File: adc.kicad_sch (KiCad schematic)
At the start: 87 parts, among them U35 MCP6004, U36 MCP6004, U46 MCP6004, U8 MCP6004

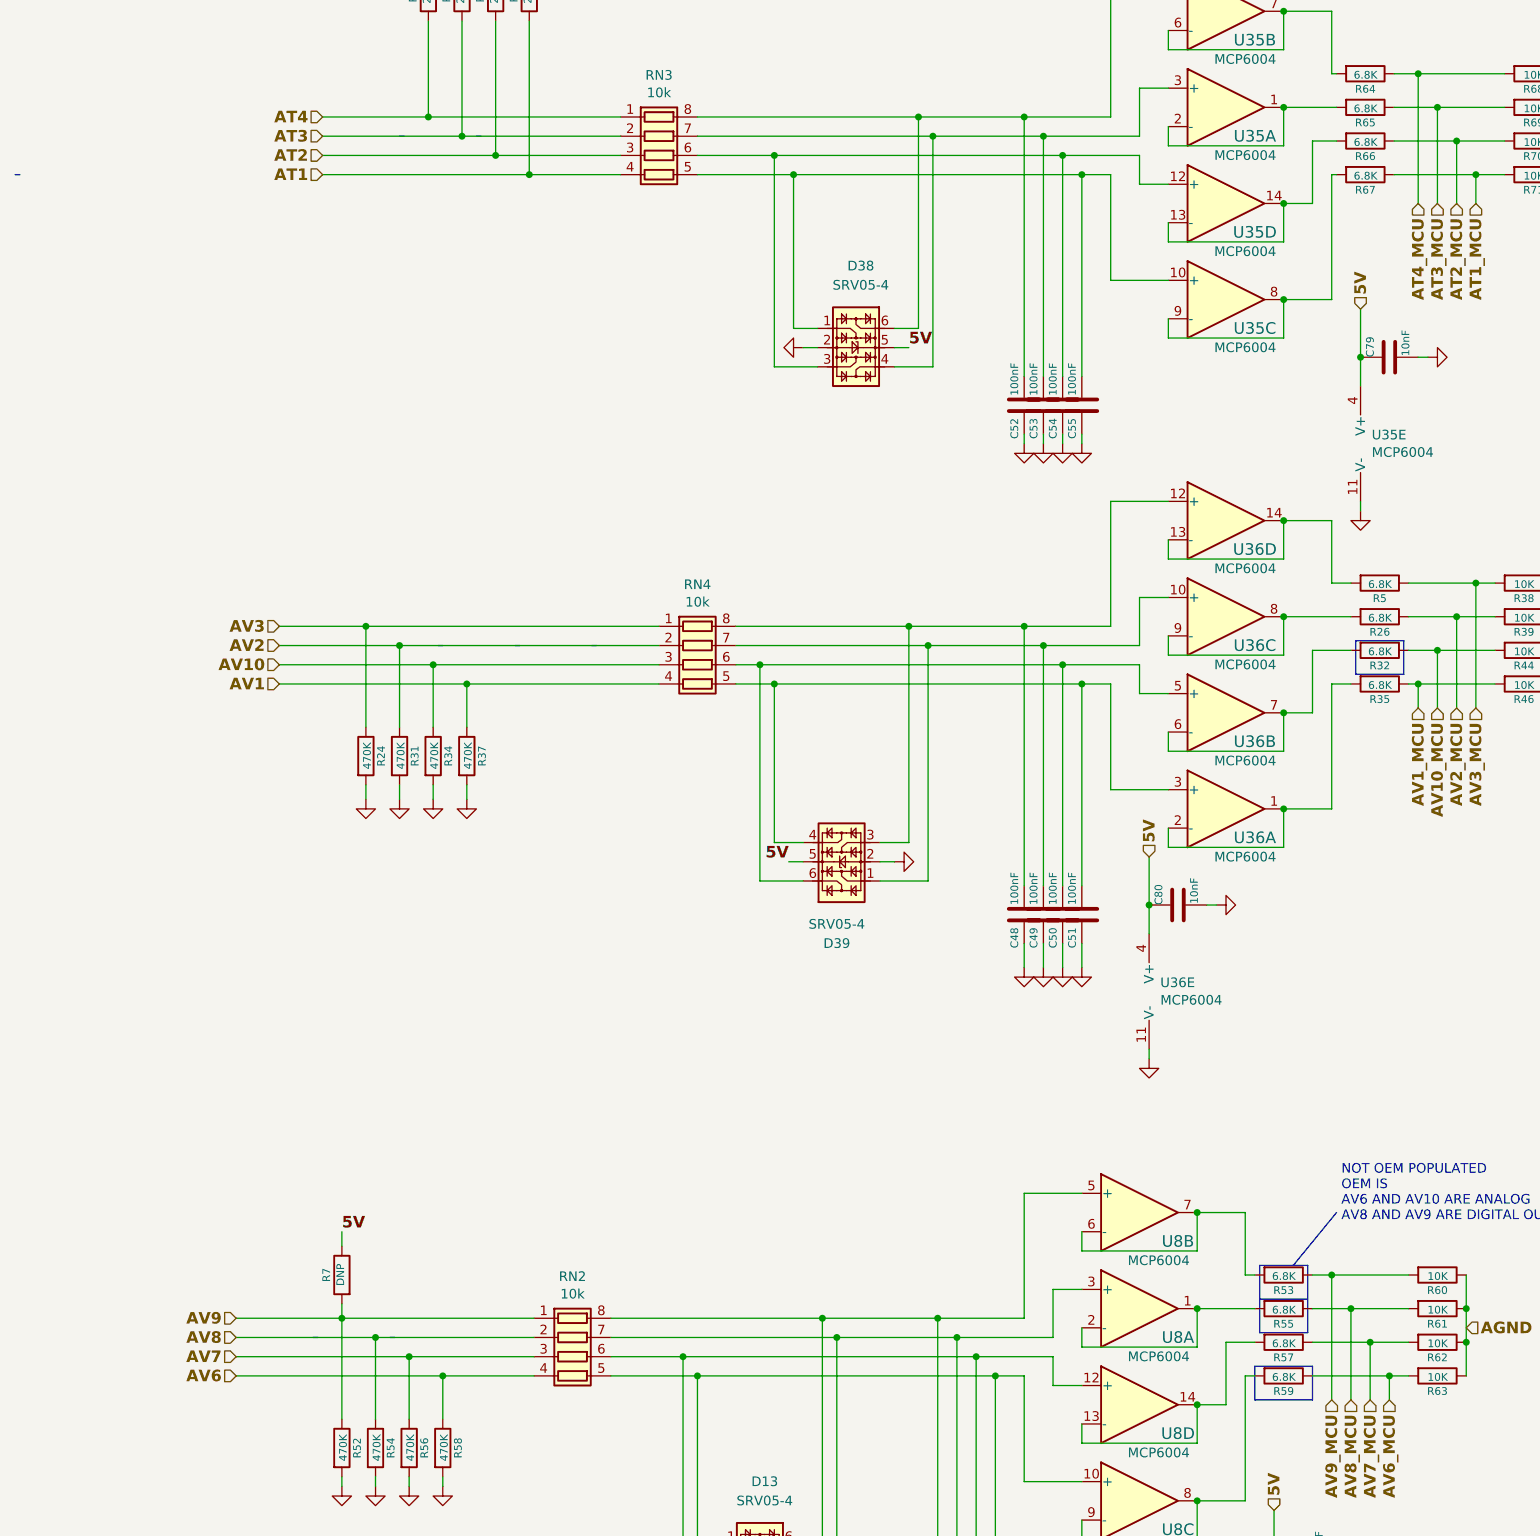
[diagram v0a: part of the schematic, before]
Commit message: replaces micro b connector by usb-c
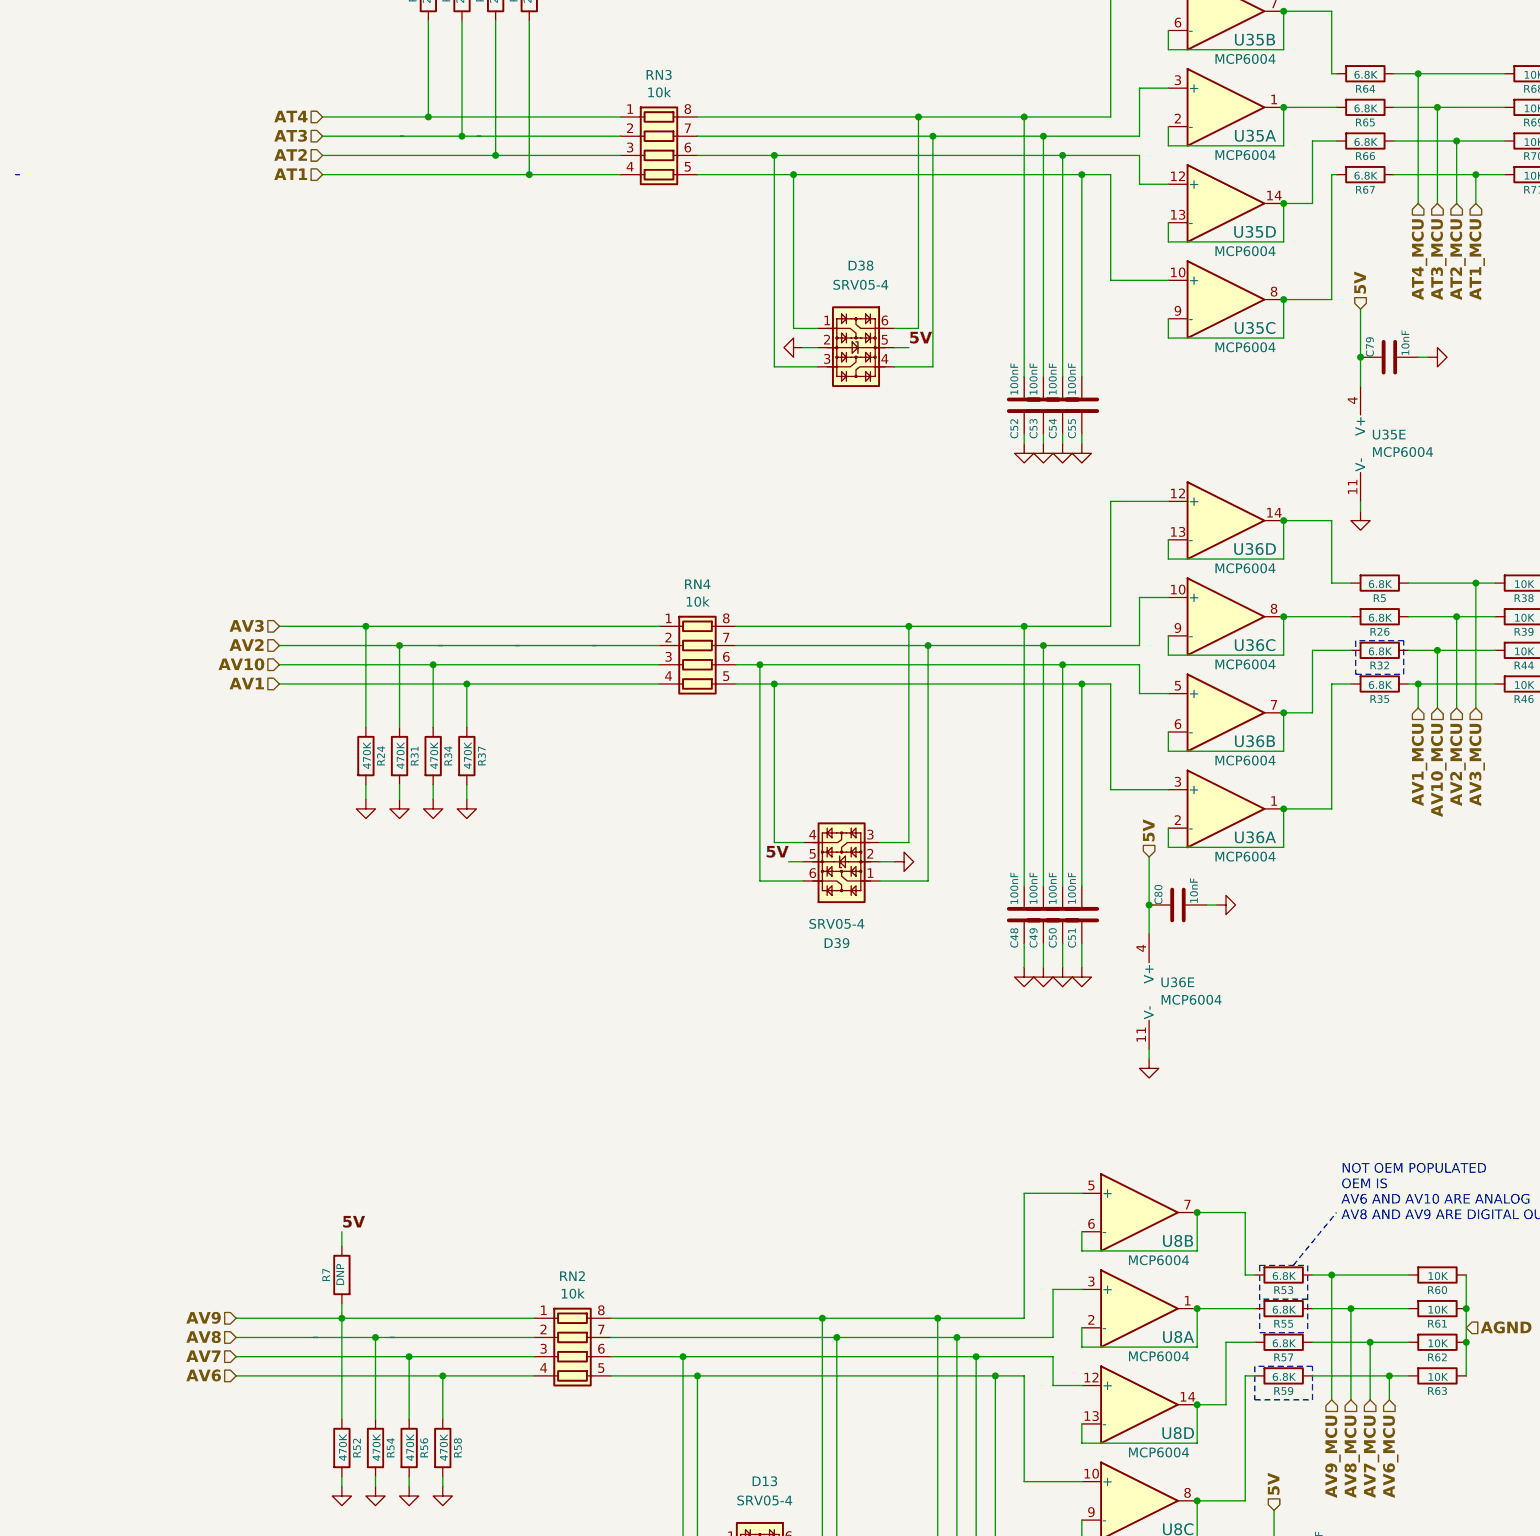
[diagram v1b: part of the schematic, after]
